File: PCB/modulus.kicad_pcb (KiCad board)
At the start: 2 copper layers, 146.3 x 95.4 mm, 55 parts, among them J1 Conn_01x09, J2 Conn_01x09, J4 Conn_01x09, J5 Conn_01x09, SW1 SW_Push, SW10 SW_Push, SW11 SW_Push, SW12 SW_Push, SW13 SW_Push, SW14 SW_Push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

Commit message: Update from M3 to M2 holes
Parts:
- REF** (x6): value MountingHole_3.2mm_M3 -> MountingHole_2.2mm_M2; footprint MountingHole:MountingHole_3.2mm_M3 -> MountingHole:MountingHole_2.2mm_M2

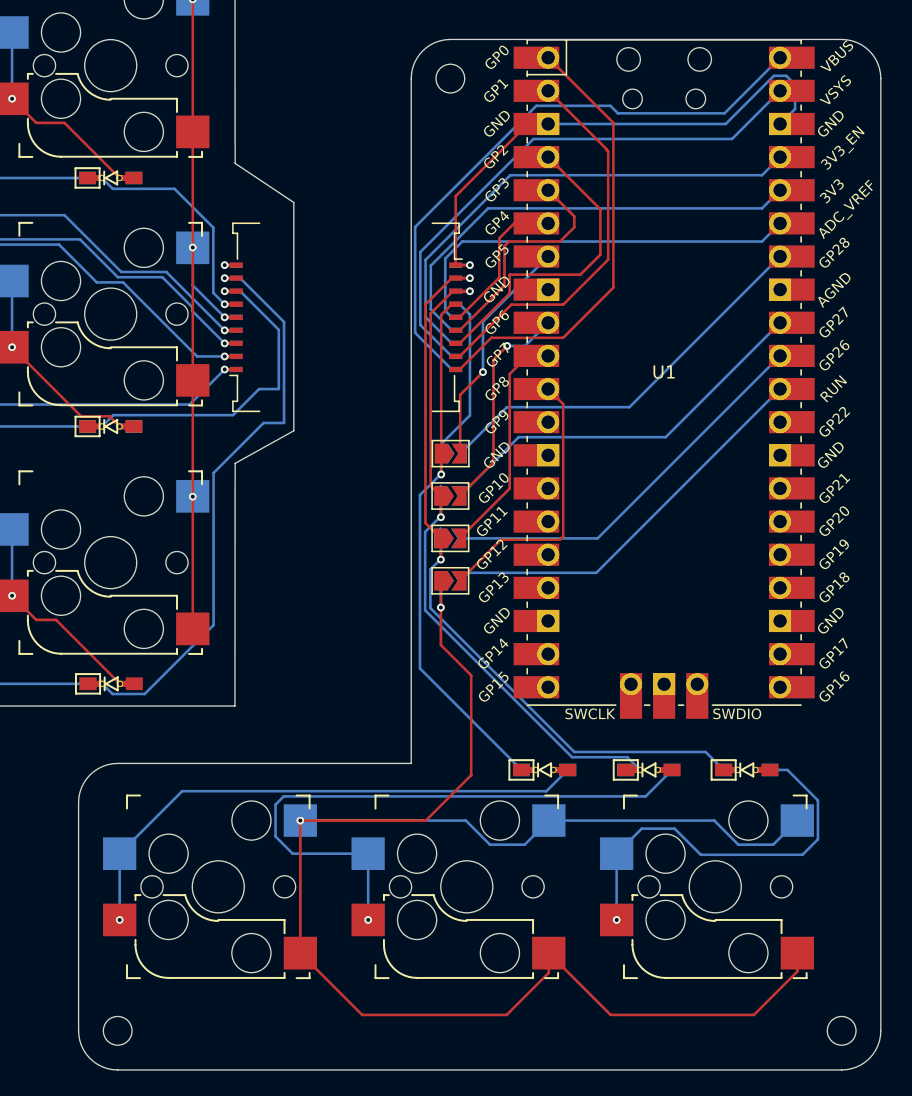
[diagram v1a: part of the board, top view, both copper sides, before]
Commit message: Minimize thumb cluster
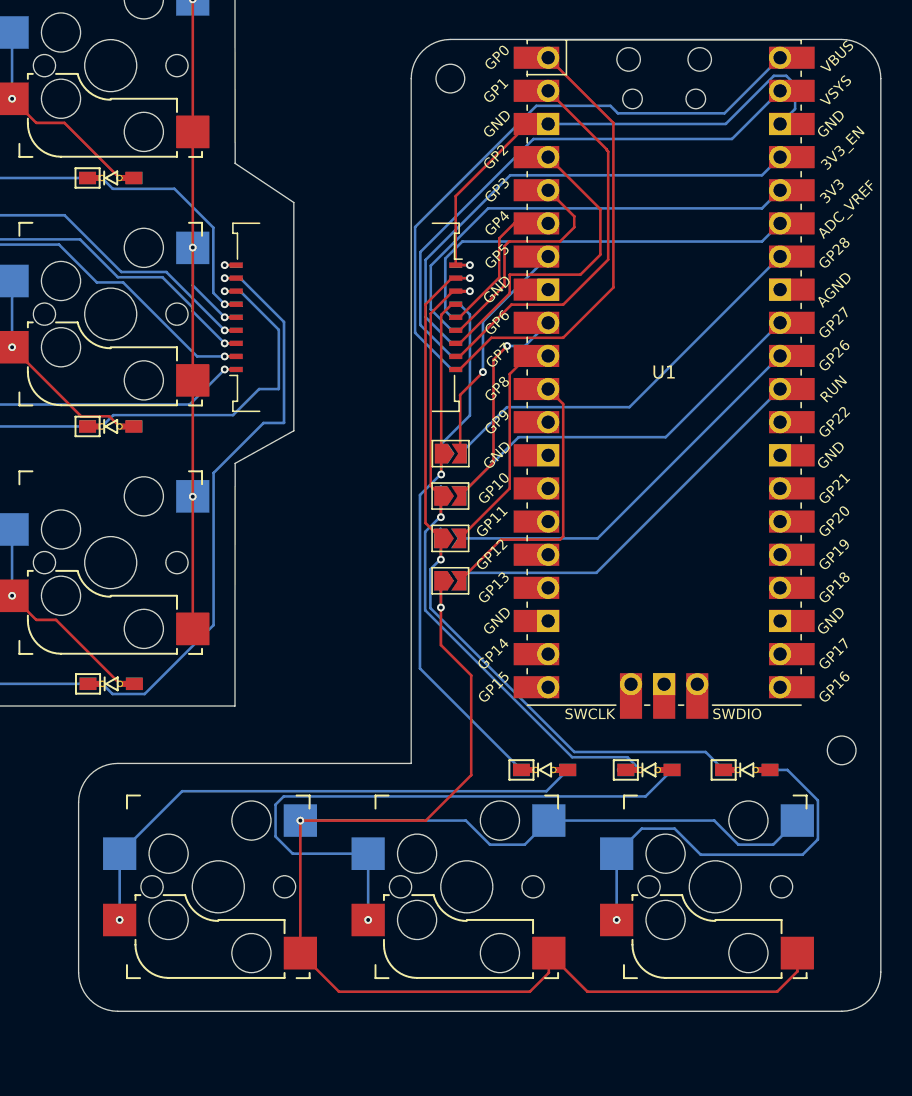
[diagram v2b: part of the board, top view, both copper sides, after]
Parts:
- removed the REF** at (145.0, 126.5)
- moved REF** 21.5 mm to (200.5, 105.0)
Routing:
- net Net-(JP7-A): track 131.4 -> 128.5 mm
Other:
- board size 146.3 x 95.4 mm -> 146.3 x 90.9 mm
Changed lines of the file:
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@@
 	(footprint "MountingHole:MountingHole_2.2mm_M2"
 		(layer "F.Cu")
-		(at 145 126.5)
-		(descr "Mounting Hole 2.2mm, no annular, M2")
-		(tags "mounting hole 2.2mm no annular m2")
-		(property "Reference" "REF**"
-			(at 0 -3.2 0)
-			(layer "F.SilkS")
-			(hide yes)
-			(effects
-				(font
-					(size 1 1)
-					(thickness 0.15)
-				)
-			)
-		)
-		(property "Value" "MountingHole_2.2mm_M2"
-			(at 0 3.2 0)
-			(layer "F.Fab")
-			(hide yes)
-			(effects
-				(font
-					(size 1 1)
-					(thickness 0.15)
-				)
-			)
-		)
-		(property "Datasheet" ""
-			(at 0 0 0)
-			(unlocked yes)
-			(layer "F.Fab")
-			(hide yes)
-			(effects
-				(font
-					(size 1.27 1.27)
-					(thickness 0.15)
-				)
-			)
-		)
-		(property "Description" ""
-			(at 0 0 0)
-			(unlocked yes)
-			(layer "F.Fab")
-			(hide yes)
-			(effects
-				(font
-					(size 1.27 1.27)
-					(thickness 0.15)
-				)
-			)
-		)
-		(attr exclude_from_pos_files exclude_from_bom)
-		(fp_circle
-			(center 0 0)
-			(end 2.2 0)
-			(stroke
-				(width 0.15)
-				(type solid)
-			)
-			(fill no)
-			(layer "Cmts.User")
-		)
-		(fp_circle
-			(center 0 0)
-			(end 2.45 0)
-			(stroke
-				(width 0.05)
-				(type solid)
-			)
-			(fill no)
-			(layer "F.CrtYd")
-		)
-		(pad "" np_thru_hole circle
-			(at 0 0)
-			(size 2.2 2.2)
-			(drill 2.2)
-			(layers "*.Cu" "*.Mask")
-		)
-		(embedded_fonts no)
-	)
-	(footprint "MountingHole:MountingHole_2.2mm_M2"
-		(layer "F.Cu")
-		(at 200.5 126.5)
+		(at 200.5 105)
 		(descr "Mounting Hole 2.2mm, no annular, M2")
 		(tags "mounting hole 2.2mm no annular m2")
@@
 		(embedded_fonts no)
 	)
+	(gr_arc
+		(start 145 125)
+		(mid 142.87868 124.12132)
+		(end 142 122)
+		(stroke
+			(width 0.05)
+			(type default)
+		)
+		(layer "Edge.Cuts")
+	)
 	(gr_line
 		(start 167.5 53.5)
@@
 		(layer "Edge.Cuts")
 	)
-	(gr_arc
-		(start 203.5 126.5)
-		(mid 202.62132 128.62132)
-		(end 200.5 129.5)
-		(stroke
-			(width 0.05)
-			(type default)
-		)
-		(layer "Edge.Cuts")
-	)
 	(gr_line
 		(start 134.14375 101.6)
@@
 	)
 	(gr_line
-		(start 145 129.5)
-		(end 200.5 129.5)
+		(start 145 125)
+		(end 200.5 125)
+		(stroke
+			(width 0.05)
+			(type default)
+		)
+		(layer "Edge.Cuts")
+	)
+	(gr_arc
+		(start 203.5 122)
+		(mid 202.62132 124.12132)
+		(end 200.5 125)
 		(stroke
 			(width 0.05)
@@
 	(gr_line
 		(start 142 109)
-		(end 142 126.5)
+		(end 142 122)
 		(stroke
 			(width 0.05)
@@
 	)
 	(gr_line
-		(start 203.5 126.5)
+		(start 203.5 122)
 		(end 203.5 53.5)
 		(stroke
@@
 		(layer "Edge.Cuts")
 	)
-	(gr_arc
-		(start 145 129.5)
-		(mid 142.87868 128.62132)
-		(end 142 126.5)
-		(stroke
-			(width 0.05)
-			(type default)
-		)
-		(layer "Edge.Cuts")
-	)
 	(gr_line
 		(start 154 83)
@@
 	)
 	(segment
-		(start 174.82 125.28)
-		(end 178.05 122.05)
+		(start 178.05 120.54)
+		(end 181.01 123.5)
 		(width 0.2)
 		(layer "F.Cu")
@@
 	(segment
 		(start 159 120.54)
-		(end 163.74 125.28)
-		(width 0.2)
-		(layer "F.Cu")
-		(net 36)
-	)
-	(segment
-		(start 182.79 125.28)
-		(end 193.776336 125.28)
+		(end 161.96 123.5)
 		(width 0.2)
 		(layer "F.Cu")
@@
 	)
 	(segment
-		(start 197.1 121.956336)
-		(end 197.1 120.54)
-		(width 0.2)
-		(layer "F.Cu")
-		(net 36)
-	)
-	(segment
-		(start 163.74 125.28)
-		(end 174.82 125.28)
+		(start 178.05 122.05)
+		(end 178.05 120.54)
 		(width 0.2)
 		(layer "F.Cu")
@@
 	)
 	(segment
-		(start 193.776336 125.28)
-		(end 197.1 121.956336)
+		(start 181.01 123.5)
+		(end 195.556336 123.5)
 		(width 0.2)
 		(layer "F.Cu")
@@
 	)
 	(segment
-		(start 178.05 122.05)
-		(end 178.05 120.54)
+		(start 161.96 123.5)
+		(end 176.6 123.5)
 		(width 0.2)
 		(layer "F.Cu")
@@
 	)
 	(segment
-		(start 178.05 120.54)
-		(end 182.79 125.28)
+		(start 197.1 121.956336)
+		(end 197.1 120.54)
+		(width 0.2)
+		(layer "F.Cu")
+		(net 36)
+	)
+	(segment
+		(start 195.556336 123.5)
+		(end 197.1 121.956336)
+		(width 0.2)
+		(layer "F.Cu")
+		(net 36)
+	)
+	(segment
+		(start 176.6 123.5)
+		(end 178.05 122.05)
 		(width 0.2)
 		(layer "F.Cu")
